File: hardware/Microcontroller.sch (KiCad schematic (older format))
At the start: 15 parts, among them J601 SWD, SW601 SW_Push, SW602 SW_Push, U601 STM32L011F4Px, Y601 32kHz

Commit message: added order references to parts
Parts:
- J601: Manufacturer (none) -> Mill-Max; Order (none) -> https://www.mouser.at/ProductDetail/Mill-Max/855-22-006-10-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
- R601, R603: Manufacturer (none) -> TE Connectivity / Holsworthy; Order (none) -> https://www.mouser.at/ProductDetail/TE-Connectivity-Holswor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
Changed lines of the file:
@@
 F 2 "Resistor_SMD:R_0603_1608Metric" H 1200 3950 50  0001 C CNN
 F 3 "~" H 1200 3950 50  0001 C CNN
+F 4 "TE Connectivity / Holsworthy" H 1200 3950 50  0001 C CNN "Manufacturer"
+F 5 "https://www.mouser.at/ProductDetail/TE-Connectivity-Holsworthy/CRGP0603F1K0?qs=sGAEpiMZZMtlubZbdhIBIOInyB5Ysv8sRTd2oyB6aAs%3D" H 1200 3950 50  0001 C CNN "Order"
 	1    1200 3950
 	0    1    1    0
@@
 F 2 "Resistor_SMD:R_0603_1608Metric" H 2400 3950 50  0001 C CNN
 F 3 "~" H 2400 3950 50  0001 C CNN
+F 4 "TE Connectivity / Holsworthy" H 2400 3950 50  0001 C CNN "Manufacturer"
+F 5 "https://www.mouser.at/ProductDetail/TE-Connectivity-Holsworthy/CRGP0603F1K0?qs=sGAEpiMZZMtlubZbdhIBIOInyB5Ysv8sRTd2oyB6aAs%3D" H 2400 3950 50  0001 C CNN "Order"
 	1    2400 3950
 	0    1    1    0
@@
 F 2 "Connector:Tag-Connect_TC2030-IDC-NL_2x03_P1.27mm_Vertical" H 4200 2800 50  0001 C CNN
 F 3 "~" H 4200 2800 50  0001 C CNN
+F 4 "Mill-Max" H 4200 2800 50  0001 C CNN "Manufacturer"
+F 5 "https://www.mouser.at/ProductDetail/Mill-Max/855-22-006-10-001101?qs=mPCt1EmoOdSJhsMqOzcHKA%3D%3D" H 4200 2800 50  0001 C CNN "Order"
 	1    4200 2800
 	1    0    0    -1

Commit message: modified bom
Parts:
- C601, C602: MNR (none) -> C0603C120K5HACTU
- C603, C604, C606, C607: MNR (none) -> C0603C104M4RACTU
- C605: MNR (none) -> CL10B106MQ8NRNC
- J601: MNR (none) -> 855-22-006-10-001101
- R601, R603: MNR (none) -> CRGP0603F1K0
- R602: MNR (none) -> CRGP0603F100K
- SW601, SW602: MNR (none) -> KMR211GLFS
- U601: MNR (none) -> STM32L011F4P6TR
- Y601: MNR (none) -> ABS07-166-32.768KHZ-T
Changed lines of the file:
@@
 F 4 "https://www.mouser.at/ProductDetail/187-CL10B106MQ8NRNC" H 3700 1600 50  0001 C CNN "Order"
 F 5 "Samsung Electro-Mechanics" H 3700 1600 50  0001 C CNN "Manufacturer"
+F 6 "CL10B106MQ8NRNC" H 3700 1600 50  0001 C CNN "MNR"
 	1    3700 1600
 	1    0    0    -1
@@
 F 4 "https://www.mouser.at/ProductDetail/80-C0603C104M4R" H 4150 1600 50  0001 C CNN "Order"
 F 5 "KEMET" H 4150 1600 50  0001 C CNN "Manufacturer"
+F 6 "C0603C104M4RACTU" H 4150 1600 50  0001 C CNN "MNR"
 	1    4150 1600
 	1    0    0    -1
@@
 F 4 "https://www.mouser.at/ProductDetail/815-ABS0716632.768KT" H 950 2300 50  0001 C CNN "Order"
 F 5 "ABRACON" H 950 2300 50  0001 C CNN "Manufacturer"
+F 6 "ABS07-166-32.768KHZ-T" H 950 2300 50  0001 C CNN "MNR"
 	1    950  2300
 	1    0    0    -1
@@
 F 4 "https://www.mouser.at/ProductDetail/80-C0603C120K5HACTU" H 600 2450 50  0001 C CNN "Order"
 F 5 "KEMET" H 600 2450 50  0001 C CNN "Manufacturer"
+F 6 "C0603C120K5HACTU" H 600 2450 50  0001 C CNN "MNR"
 	1    600  2450
 	1    0    0    -1
@@
 F 4 "https://www.mouser.at/ProductDetail/80-C0603C120K5HACTU" H 1300 2450 50  0001 C CNN "Order"
 F 5 "KEMET" H 1300 2450 50  0001 C CNN "Manufacturer"
+F 6 "C0603C120K5HACTU" H 1300 2450 50  0001 C CNN "MNR"
 	1    1300 2450
 	1    0    0    -1
@@
 F 4 "https://www.mouser.at/ProductDetail/80-C0603C104M4R" H 4600 1600 50  0001 C CNN "Order"
 F 5 "KEMET" H 4600 1600 50  0001 C CNN "Manufacturer"
+F 6 "C0603C104M4RACTU" H 4600 1600 50  0001 C CNN "MNR"
 	1    4600 1600
 	1    0    0    -1
@@
 F 4 "https://www.mouser.at/ProductDetail/80-C0603C104M4R" H 1450 4200 50  0001 C CNN "Order"
 F 5 "KEMET" H 1450 4200 50  0001 C CNN "Manufacturer"
+F 6 "C0603C104M4RACTU" H 1450 4200 50  0001 C CNN "MNR"
 	1    1450 4200
 	1    0    0    -1
@@
 F 4 "https://www.mouser.at/ProductDetail/611-KMR211G-LFS" V 950 4200 50  0001 C CNN "Order"
 F 5 "C&K" H 950 4200 50  0001 C CNN "Manufacturer"
+F 6 "KMR211GLFS" H 950 4200 50  0001 C CNN "MNR"
 	1    950  4200
 	0    -1   -1   0
@@
 F 4 "https://www.mouser.at/ProductDetail/80-C0603C104M4R" H 2650 4200 50  0001 C CNN "Order"
 F 5 "KEMET" H 2650 4200 50  0001 C CNN "Manufacturer"
+F 6 "C0603C104M4RACTU" H 2650 4200 50  0001 C CNN "MNR"
 	1    2650 4200
 	1    0    0    -1
@@
 F 4 "https://www.mouser.at/ProductDetail/611-KMR211G-LFS" V 2150 4200 50  0001 C CNN "Order"
 F 5 "C&K" H 2150 4200 50  0001 C CNN "Manufacturer"
+F 6 "KMR211GLFS" H 2150 4200 50  0001 C CNN "MNR"
 	1    2150 4200
 	0    -1   -1   0
@@
 F 4 "https://www.mouser.at/ProductDetail/511-STM32L011F4P6TR" H 2300 2200 50  0001 C CNN "Order"
 F 5 "STMicroelectornics" H 2300 2200 50  0001 C CNN "Manufacturer"
+F 6 "STM32L011F4P6TR" H 2300 2200 50  0001 C CNN "MNR"
 	1    2300 2200
 	1    0    0    -1
@@
 F 4 "https://www.mouser.at/ProductDetail/279-CRGP0603F100K" H 1550 3000 50  0001 C CNN "Order"
 F 5 "TE Connectivity / Holsworthy" H 1550 3000 50  0001 C CNN "Manufacturer"
+F 6 "CRGP0603F100K" H 1550 3000 50  0001 C CNN "MNR"
 	1    1550 3000
 	1    0    0    -1
@@
 F 4 "TE Connectivity / Holsworthy" H 1200 3950 50  0001 C CNN "Manufacturer"
 F 5 "https://www.mouser.at/ProductDetail/TE-Connectivity-Holsworthy/CRGP0603F1K0?qs=sGAEpiMZZMtlubZbdhIBIOInyB5Ysv8sRTd2oyB6aAs%3D" H 1200 3950 50  0001 C CNN "Order"
+F 6 "CRGP0603F1K0" H 1200 3950 50  0001 C CNN "MNR"
 	1    1200 3950
 	0    1    1    0
@@
 F 4 "TE Connectivity / Holsworthy" H 2400 3950 50  0001 C CNN "Manufacturer"
 F 5 "https://www.mouser.at/ProductDetail/TE-Connectivity-Holsworthy/CRGP0603F1K0?qs=sGAEpiMZZMtlubZbdhIBIOInyB5Ysv8sRTd2oyB6aAs%3D" H 2400 3950 50  0001 C CNN "Order"
+F 6 "CRGP0603F1K0" H 2400 3950 50  0001 C CNN "MNR"
 	1    2400 3950
 	0    1    1    0
@@
 F 4 "Mill-Max" H 4200 2800 50  0001 C CNN "Manufacturer"
 F 5 "https://www.mouser.at/ProductDetail/Mill-Max/855-22-006-10-001101?qs=mPCt1EmoOdSJhsMqOzcHKA%3D%3D" H 4200 2800 50  0001 C CNN "Order"
+F 6 "855-22-006-10-001101" H 4200 2800 50  0001 C CNN "MNR"
 	1    4200 2800
 	1    0    0    -1

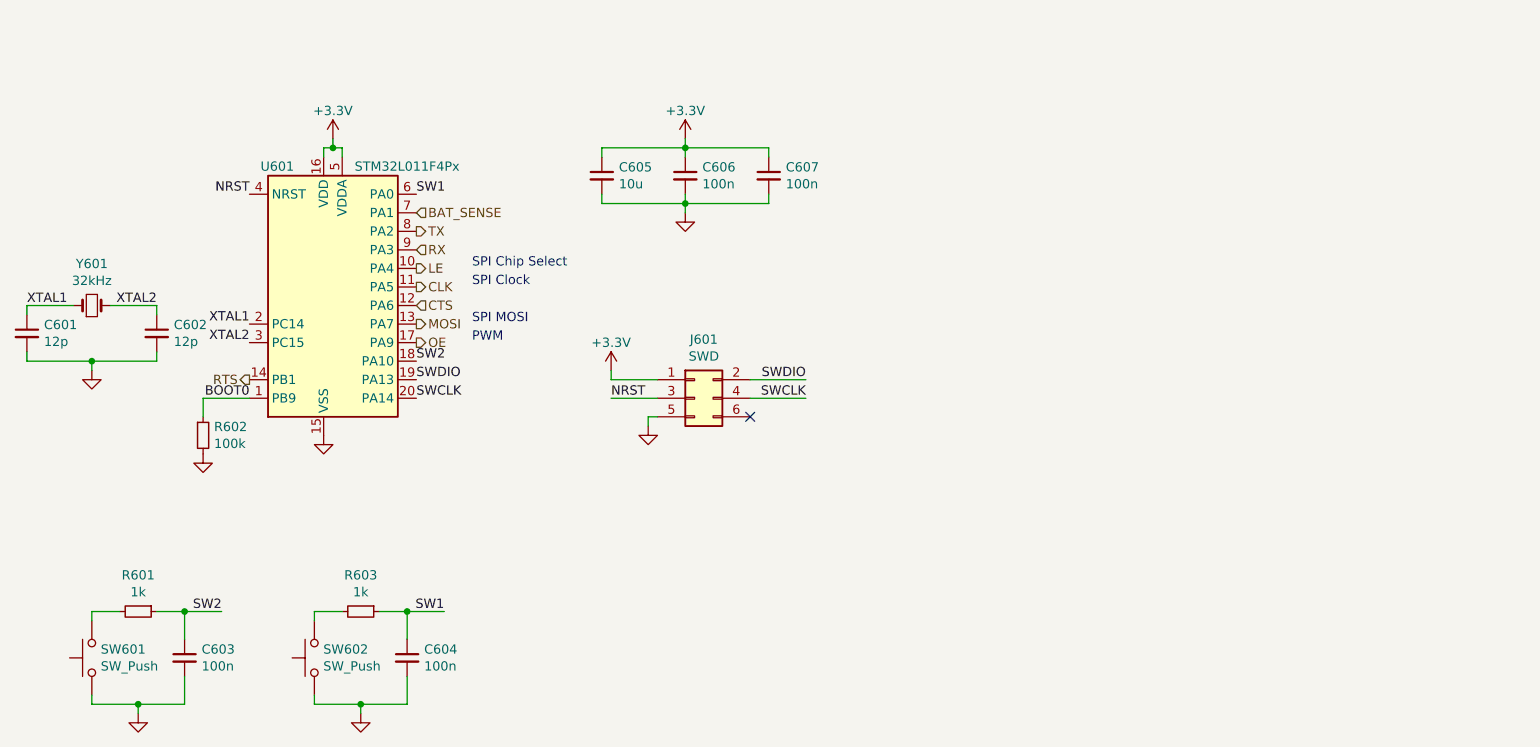
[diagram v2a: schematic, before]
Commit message: New uC, ditched FTDI chip, and more!
Need to improve the schematic a little bit more.
For example, I want to be able to turn the LED Drivers off using
a MOSFET.

For the PCB Layout: I want to move as many components as possible
to the top layer, so that they are visible when in the case.
Also, I have to consider solderability of the components, the more
complex should all be on one layer for easier soldering.

Next up: Finishing the schematic, improving component placement,
and routing!
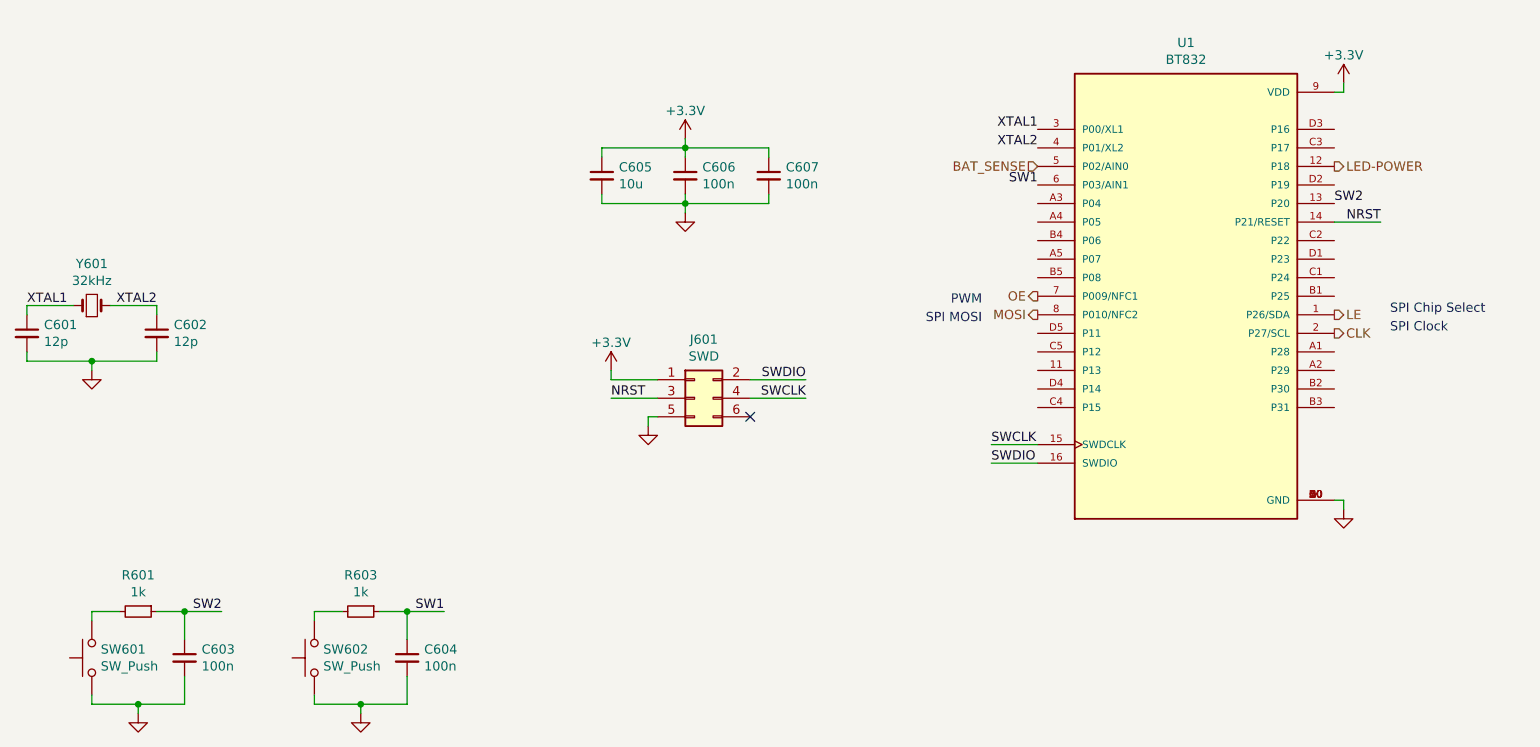
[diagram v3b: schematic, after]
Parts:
- removed R602: 100k, Resistor_SMD:R_0603_1608Metric, symbol Device:R_Small
- removed U601: STM32L011F4Px, Package_SO:TSSOP-20_4.4x6.5mm_P0.65mm, symbol MCU_ST_STM32L0:STM32L011F4Px
- added U1: BT832, watch:BLEMODULE_BT832, symbol watch:BT832
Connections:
- net +3V3: now also U1.9 (VDD)
- net BAT_SENSE: now also U1.5 (P02/AIN0)
- net CLK: now also U1.2 (P27/SCL)
- net GND: now also U1.10 (GND), U1.A0 (GND), U1.B0 (GND), U1.C0 (GND), U1.D0 (GND)
- net LE: now also U1.1 (P26/SDA)
- net MOSI: now also U1.8 (P010/NFC2)
- net NRST: now also U1.14 (P21/RESET)
- net OE: now also U1.7 (P009/NFC1)
- net SW1: now also U1.6 (P03/AIN1)
- net SW2: now also U1.13 (P20)
- net SWCLK: now also U1.15 (SWDCLK)
- net SWDIO: now also U1.16 (SWDIO)
- net XTAL1: now also U1.3 (P00/XL1)
- net XTAL2: now also U1.4 (P01/XL2)
- new net LED-POWER: U1.12 (P18)
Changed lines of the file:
@@
 $Descr A4 11693 8268
 encoding utf-8
-Sheet 6 7
+Sheet 6 6
 Title "aWristWatch"
 Date "2021-04-05"
@@
 	0    -1   -1   0
 $EndComp
-$Comp
-L power:GND #PWR?
-U 1 1 605DDD89
-P 2200 3000
-AR Path="/605DDD89" Ref="#PWR?"  Part="1"
-AR Path="/605DA130/605DDD89" Ref="#PWR0144"  Part="1"
-F 0 "#PWR0144" H 2200 2750 50  0001 C CNN
-F 1 "GND" H 2205 2827 50  0001 C CNN
-F 2 "" H 2200 3000 50  0001 C CNN
-F 3 "" H 2200 3000 50  0001 C CNN
-	1    2200 3000
-	1    0    0    -1
-$EndComp
-Text Label 2700 2700 0    50   ~ 0
-SWDIO
-Text Label 2700 2800 0    50   ~ 0
-SWCLK
-$Comp
-L MCU_ST_STM32L0:STM32L011F4Px U?
-U 1 1 605DDD97
-P 2300 2200
-AR Path="/605DDD97" Ref="U?"  Part="1"
-AR Path="/605DA130/605DDD97" Ref="U601"  Part="1"
-F 0 "U601" H 1950 2850 50  0000 C CNN
-F 1 "STM32L011F4Px" H 2650 2850 50  0000 C CNN
-F 2 "Package_SO:TSSOP-20_4.4x6.5mm_P0.65mm" H 1900 1500 50  0001 R CNN
-F 3 "http://www.st.com/st-web-ui/static/active/en/resource/technical/document/datasheet/DM00206508.pdf" H 2300 2200 50  0001 C CNN
-F 4 "https://www.mouser.at/ProductDetail/511-STM32L011F4P6TR" H 2300 2200 50  0001 C CNN "Order"
-F 5 "STMicroelectornics" H 2300 2200 50  0001 C CNN "Manufacturer"
-F 6 "STM32L011F4P6TR" H 2300 2200 50  0001 C CNN "MNR"
-	1    2300 2200
-	1    0    0    -1
-$EndComp
-Wire Wire Line
-	2200 1450 2200 1500
-Wire Wire Line
-	2300 1450 2300 1500
-Wire Wire Line
-	2250 1450 2300 1450
-Wire Wire Line
-	2250 1450 2200 1450
-Connection ~ 2250 1450
-$Comp
-L power:+3.3V #PWR?
-U 1 1 605DDDA2
-P 2250 1400
-AR Path="/605DDDA2" Ref="#PWR?"  Part="1"
-AR Path="/605DA130/605DDDA2" Ref="#PWR0145"  Part="1"
-F 0 "#PWR0145" H 2250 1250 50  0001 C CNN
-F 1 "+3.3V" H 2250 1550 50  0000 C CNN
-F 2 "" H 2250 1400 50  0001 C CNN
-F 3 "" H 2250 1400 50  0001 C CNN
-	1    2250 1400
-	1    0    0    -1
-$EndComp
-Wire Wire Line
-	2250 1400 2250 1450
-Text Notes 3000 2100 0    50   ~ 0
+Text Notes 7950 2350 0    50   ~ 0
 SPI Chip Select
-Text Notes 3000 2200 0    50   ~ 0
+Text Notes 7950 2450 0    50   ~ 0
 SPI Clock
-Text Notes 3000 2400 0    50   ~ 0
+Text Notes 5750 2400 2    50   ~ 0
 SPI MOSI
-Text Notes 3000 2500 0    50   ~ 0
+Text Notes 5750 2300 2    50   ~ 0
 PWM
-Text Label 2700 1700 0    50   ~ 0
+Text Label 6050 1650 2    50   ~ 0
 SW1
-Text Label 2700 2600 0    50   ~ 0
+Text Label 7650 1750 0    50   ~ 0
 SW2
-Text Label 1800 1700 2    50   ~ 0
-NRST
-Text Label 1800 2400 2    50   ~ 0
+Text Label 6050 1350 2    50   ~ 0
 XTAL1
-Text Label 1800 2500 2    50   ~ 0
+Text Label 6050 1450 2    50   ~ 0
 XTAL2
-$Comp
-L power:GND #PWR?
-U 1 1 605DDDC3
-P 1550 3100
-AR Path="/605DDDC3" Ref="#PWR?"  Part="1"
-AR Path="/605DA130/605DDDC3" Ref="#PWR0146"  Part="1"
-F 0 "#PWR0146" H 1550 2850 50  0001 C CNN
-F 1 "GND" H 1555 2927 50  0001 C CNN
-F 2 "" H 1550 3100 50  0001 C CNN
-F 3 "" H 1550 3100 50  0001 C CNN
-	1    1550 3100
-	1    0    0    -1
-$EndComp
-$Comp
-L Device:R_Small R?
-U 1 1 605DDDCA
-P 1550 3000
-AR Path="/605DDDCA" Ref="R?"  Part="1"
-AR Path="/605DA130/605DDDCA" Ref="R602"  Part="1"
-F 0 "R602" H 1609 3046 50  0000 L CNN
-F 1 "100k" H 1609 2955 50  0000 L CNN
-F 2 "Resistor_SMD:R_0603_1608Metric" H 1550 3000 50  0001 C CNN
-F 3 "https://www.mouser.at/datasheet/2/418/5/NG_DS_9-1773463-9_A-1358566.pdf" H 1550 3000 50  0001 C CNN
-F 4 "https://www.mouser.at/ProductDetail/279-CRGP0603F100K" H 1550 3000 50  0001 C CNN "Order"
-F 5 "TE Connectivity / Holsworthy" H 1550 3000 50  0001 C CNN "Manufacturer"
-F 6 "CRGP0603F100K" H 1550 3000 50  0001 C CNN "MNR"
-	1    1550 3000
-	1    0    0    -1
-$EndComp
 $Comp
 L Device:R_Small R601
@@
 	2850 3950 2650 3950
 Connection ~ 2650 3950
-Text HLabel 2700 2100 2    50   Output ~ 0
+Text HLabel 7650 2350 2    50   Output ~ 0
 LE
-Text HLabel 2700 2200 2    50   Output ~ 0
+Text HLabel 7650 2450 2    50   Output ~ 0
 CLK
-Text HLabel 2700 2400 2    50   Output ~ 0
+Text HLabel 6050 2350 0    50   Output ~ 0
 MOSI
-Text HLabel 2700 2500 2    50   Output ~ 0
+Text HLabel 6050 2250 0    50   Output ~ 0
 OE
-Text HLabel 2700 1800 2    50   Input ~ 0
+Text HLabel 6050 1550 0    50   Input ~ 0
 BAT_SENSE
-Wire Wire Line
-	1550 2800 1800 2800
-Wire Wire Line
-	1550 2800 1550 2900
-Text HLabel 2700 1900 2    50   Output ~ 0
-TX
-Text HLabel 2700 2000 2    50   Input ~ 0
-RX
-Text HLabel 2700 2300 2    50   Input ~ 0
-CTS
-Text Label 1800 2800 2    50   ~ 0
-BOOT0
-Text HLabel 1800 2700 0    50   Output ~ 0
-RTS
 $Comp
 L Connector_Generic:Conn_02x03_Odd_Even J601
@@
 	3950 2900 4000 2900
 NoConn ~ 4500 2900
+$Comp
+L watch:BT832 U1
+U 1 1 61900ECF
+P 6850 2250
+F 0 "U1" H 6850 3617 50  0000 C CNN
+F 1 "BT832" H 6850 3526 50  0000 C CNN
+F 2 "watch:BLEMODULE_BT832" H 6850 2250 50  0001 L BNN
+F 3 "" H 6850 2250 50  0001 L BNN
+F 4 "Manufacturer Recommendations" H 6850 2250 50  0001 L BNN "STANDARD"
+F 5 "FANSTEL" H 6850 2250 50  0001 L BNN "MANUFACTURER"
+F 6 "2.04" H 6850 2250 50  0001 L BNN "PARTREV"
+	1    6850 2250
+	1    0    0    -1
+$EndComp
+$Comp
+L power:+3.3V #PWR?
+U 1 1 61905ED1
+P 7700 1100
+AR Path="/61905ED1" Ref="#PWR?"  Part="1"
+AR Path="/605DA130/61905ED1" Ref="#PWR0144"  Part="1"
+F 0 "#PWR0144" H 7700 950 50  0001 C CNN
+F 1 "+3.3V" H 7700 1250 50  0000 C CNN
+F 2 "" H 7700 1100 50  0001 C CNN
+F 3 "" H 7700 1100 50  0001 C CNN
+	1    7700 1100
+	1    0    0    -1
+$EndComp
+Wire Wire Line
+	7700 1100 7700 1150
+Wire Wire Line
+	7700 1150 7650 1150
+$Comp
+L power:GND #PWR?
+U 1 1 61906EDA
+P 7700 3400
+AR Path="/61906EDA" Ref="#PWR?"  Part="1"
+AR Path="/605DA130/61906EDA" Ref="#PWR0145"  Part="1"
+F 0 "#PWR0145" H 7700 3150 50  0001 C CNN
+F 1 "GND" H 7705 3227 50  0001 C CNN
+F 2 "" H 7700 3400 50  0001 C CNN
+F 3 "" H 7700 3400 50  0001 C CNN
+	1    7700 3400
+	1    0    0    -1
+$EndComp
+Wire Wire Line
+	7700 3400 7700 3350
+Wire Wire Line
+	7700 3350 7650 3350
+Text Label 5800 3150 0    50   ~ 0
+SWDIO
+Text Label 5800 3050 0    50   ~ 0
+SWCLK
+Wire Wire Line
+	5800 3050 6050 3050
+Wire Wire Line
+	6050 3150 5800 3150
+Text Label 7900 1850 2    50   ~ 0
+NRST
+Wire Wire Line
+	7900 1850 7650 1850
+Text HLabel 7650 1550 2    50   Output ~ 0
+LED-POWER
 $EndSCHEMATC

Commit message: Updated to KiCad v6.0
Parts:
- SW601, SW602: MNR KMR211GLFS -> TAC-35N-V-T/R; Manufacturer C&K -> Diptronics; Order https://www.mouser.at/ProductDetail/611-KMR211G-LFS -> https://www.mouser.at/ProductDetail/Diptronics/TAC-35N-V-T-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
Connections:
- net +3V3 renamed VIN
- net LED-POWER renamed LED_POWER_CTL
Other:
- moved on the sheet: C605, C606, C607, J601, U1
